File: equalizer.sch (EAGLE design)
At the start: 34 parts

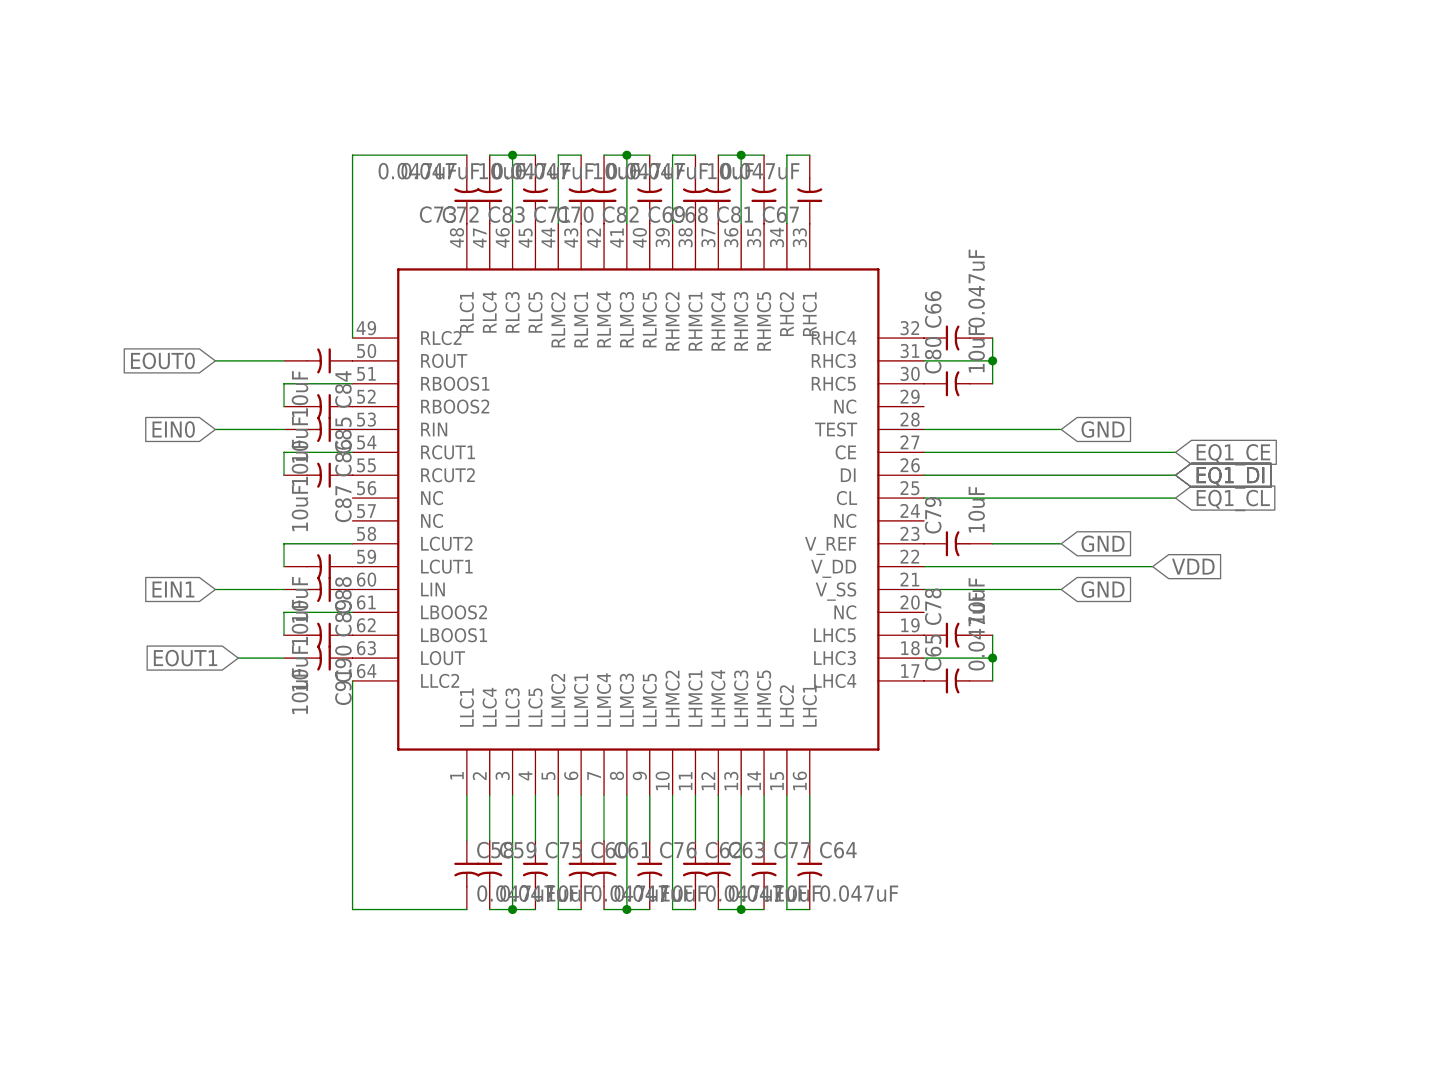
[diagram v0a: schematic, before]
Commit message: rm cache files, add boards for components
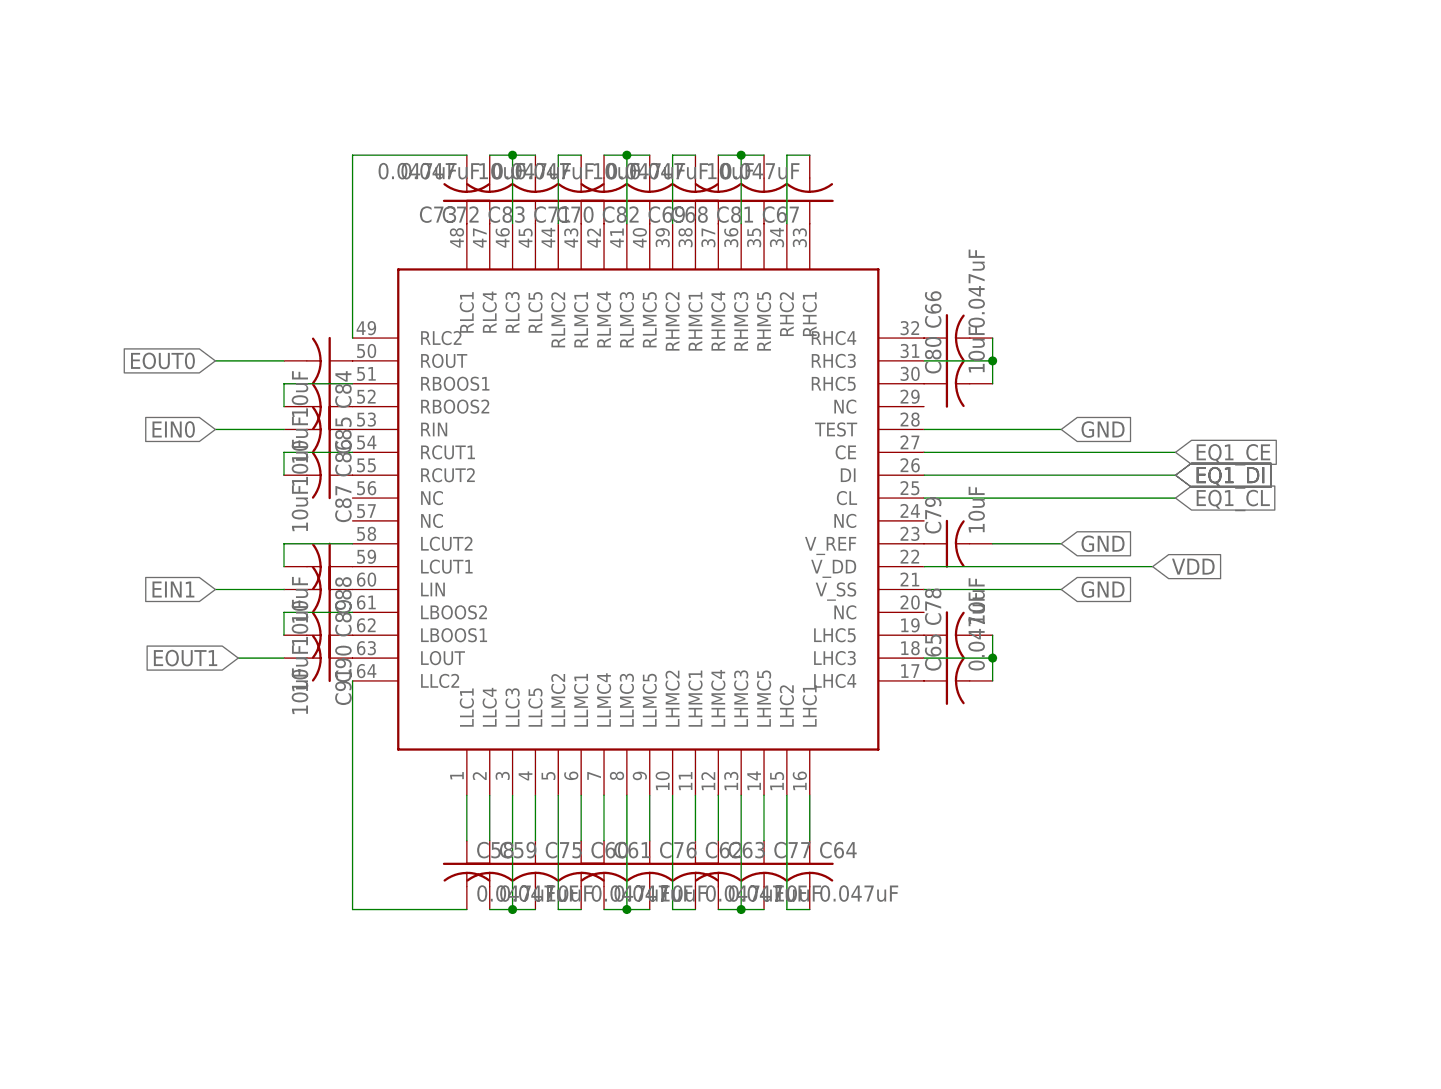
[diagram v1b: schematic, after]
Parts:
- C58, C59, C60, C61, C62, C63, C64, C65, C66, C67, C68, C69, C70, C71, C72, C73, C75, C76, C77, C78, C79, C80, C81, C82, C83, C84, C85, C86, C87, C88, C89, C90, C91: device rcl:C-US025-024X044 -> rcl:C-USC0402

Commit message: corrections
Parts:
- removed C86, C89: 10uF, rcl:C-USC0402
- added C1: 10uF, rcl:C-USC0402
- added CE_EQ, CL_EQ, DI_EQ: (no value), wirepad:SMD2
- C60, C61, C64, C65, C66, C67, C70, C71: value 0.047uF -> 0.01uF
- C62, C63, C68, C69: value 0.047uF -> 0.068uF
- C84, C91: value 10uF -> 0.1uF
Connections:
- removed net N$199: C86.1, U$14.RIN
- removed net N$202: C89.1, U$14.LIN
- net EIN0: now also U$14.RIN; no longer C86.2
- net EIN1: now also U$14.LIN; no longer C89.2
- net EQ1_CE: now also CE_EQ.P
- net EQ1_CL: now also CL_EQ.P
- net EQ1_DI: now also DI_EQ.P
- net GND: now also C1.2
- net N$192: now also C1.1
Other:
- moved on the sheet: C58, C59, C61, C63, C65, C66, C68, C70, C72, C75, C76, C77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

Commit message: updates
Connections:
- net EIN0 renamed IN1_EQ
- net EIN1 renamed IN2_EQ
- net EOUT0 renamed OUT1_EQ
- net EOUT1 renamed OUT2_EQ
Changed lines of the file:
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@@
 </segment>
 </net>
-<net name="EIN0" class="0">
+<net name="IN1_EQ" class="0">
 <segment>
 <label x="-2.54" y="53.34" size="1.778" layer="95" rot="R180" xref="yes"/>
@@
 </segment>
 </net>
-<net name="EIN1" class="0">
+<net name="IN2_EQ" class="0">
 <segment>
 <label x="-5.08" y="35.56" size="1.778" layer="95" rot="R180" xref="yes"/>
@@
 </segment>
 </net>
-<net name="EOUT0" class="0">
+<net name="OUT1_EQ" class="0">
 <segment>
 <pinref part="C84" gate="G$1" pin="2"/>
@@
 </segment>
 </net>
-<net name="EOUT1" class="0">
+<net name="OUT2_EQ" class="0">
 <segment>
 <pinref part="C91" gate="G$1" pin="2"/>
